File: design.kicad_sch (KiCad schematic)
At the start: 0 parts

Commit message: add TPS61099
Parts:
- added U1: TPS61099YFFT, BGA6N40P3X2_122X88X62N, symbol Converter_DCDC_custom:TPS61099YFFT
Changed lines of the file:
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@@
     (comment 4 "<<hash>>")
+  )
+  (symbol (lib_id "Converter_DCDC_custom:TPS61099YFFT") (at 147.32 88.9 0) (unit 1)
+    (in_bom yes) (on_board yes) (fields_autoplaced)
+    (property "Reference" "U1" (id 0) (at 147.32 76.2 0))
+    (property "Value" "TPS61099YFFT" (id 1) (at 147.32 78.74 0))
+    (property "Footprint" "BGA6N40P3X2_122X88X62N" (id 2) (at 147.32 81.28 0)
+      (effects (font (size 1.27 1.27)) (justify left bottom) hide)
+    )
+    (property "Datasheet" "" (id 3) (at 147.32 88.9 0)
+      (effects (font (size 1.27 1.27)) (justify left bottom) hide)
+    )
+    (property "STANDARD" "IPC 7351B" (id 4) (at 147.32 73.66 0)
+      (effects (font (size 1.27 1.27)) (justify left bottom) hide)
+    )
+    (property "PARTREV" "K" (id 5) (at 144.78 76.2 0)
+      (effects (font (size 1.27 1.27)) (justify left bottom) hide)
+    )
+    (property "MAXIMUM_PACKAGE_HEIGHT" "0.625mm" (id 6) (at 147.32 76.2 0)
+      (effects (font (size 1.27 1.27)) (justify left bottom) hide)
+    )
+    (property "MANUFACTURER" "Texas Instruments" (id 7) (at 147.32 78.74 0)
+      (effects (font (size 1.27 1.27)) (justify left bottom) hide)
+    )
+    (pin "A1")
+    (pin "A2")
+    (pin "B1")
+    (pin "B2")
+    (pin "C1")
+    (pin "C2")
   )
   (sheet_instances
     (path "/" (page "1"))
   )
+  (symbol_instances
+    (path "/63f96008-1e4e-43d2-a021-cfff672ef086"
+      (reference "U1") (unit 1) (value "TPS61099YFFT") (footprint "BGA6N40P3X2_122X88X62N")
+    )
+  )
 )

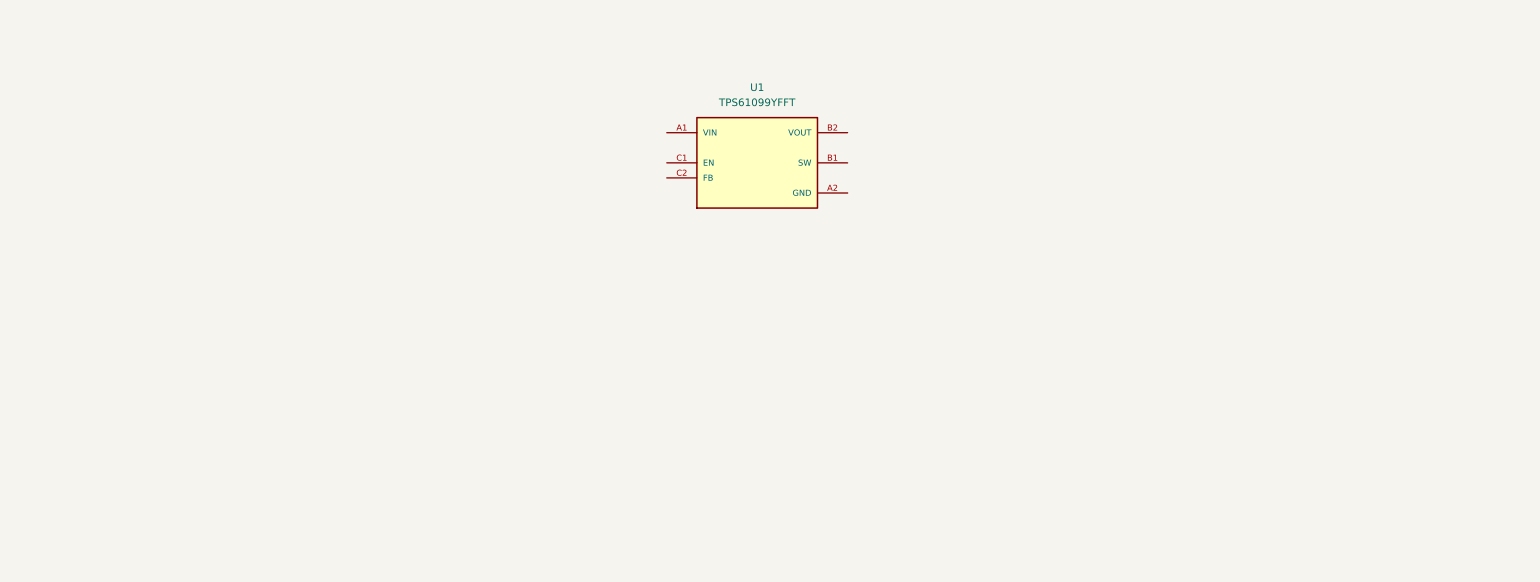
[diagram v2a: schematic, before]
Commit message: SCH/PCB Add initial design
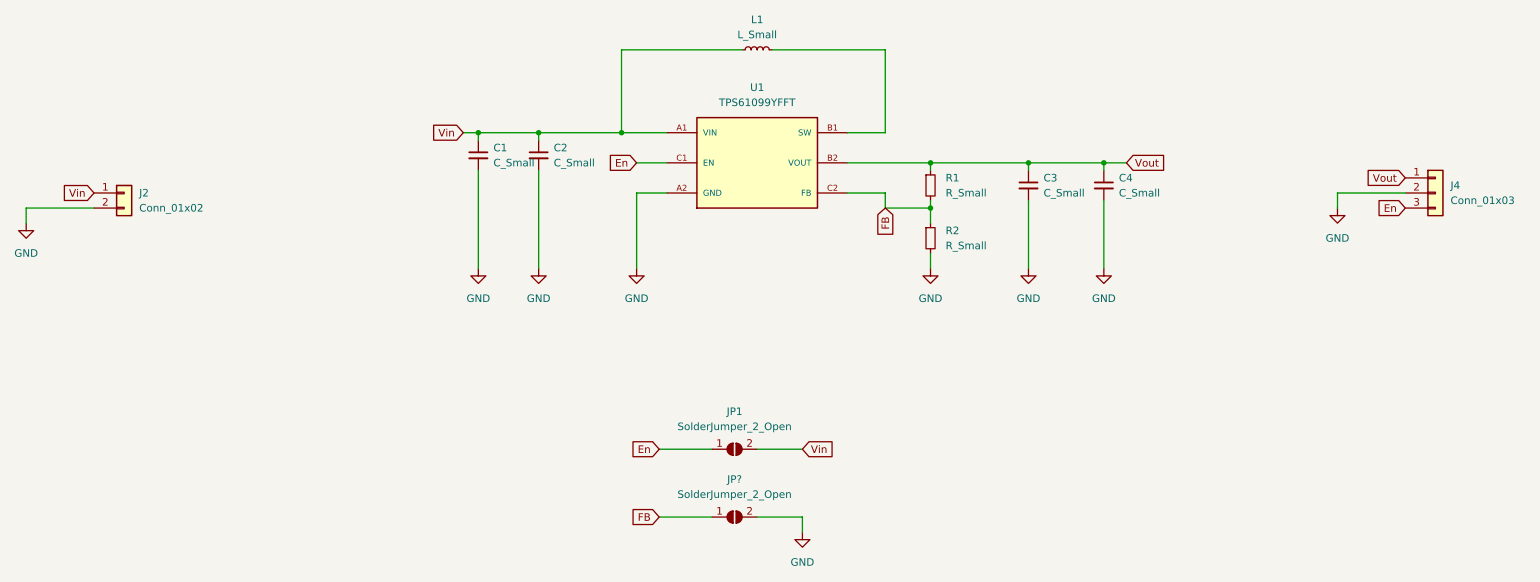
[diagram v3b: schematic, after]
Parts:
- added C1, C2, C3, C4: C_Small, Capacitor_SMD:C_0805_2012Metric, symbol Device:C_Small
- added J2: Conn_01x02, Connector_PinHeader_2.54mm:PinHeader_1x02_P2.54mm_Vertical, symbol Connector_Generic:Conn_01x02
- added J4: Conn_01x03, Connector_PinHeader_2.54mm:PinHeader_1x03_P2.54mm_Vertical, symbol Connector_Generic:Conn_01x03
- added JP1, JP?: SolderJumper_2_Open, Jumper:SolderJumper-2_P1.3mm_Open_RoundedPad1.0x1.5mm, symbol Jumper:SolderJumper_2_Open
- added L1: L_Small, Inductor_SMD:L_1008_2520Metric, symbol Device:L_Small
- added R1, R2: R_Small, Resistor_SMD:R_0805_2012Metric, symbol Device:R_Small
- U1: footprint BGA6N40P3X2_122X88X62N -> Converter_DCDC_custom:BGA6N40P3X2_122X88X62N
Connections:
- net Vin: now reaches U1.A1 (VIN)
- net Vin: now also C1.1, C2.1, J2.1 (Pin_1), JP1.2 (B), L1.1
- net GND: now reaches U1.A2 (GND)
- net GND: now also C1.2, C2.2, C3.2, C4.2, J2.2 (Pin_2), J4.2 (Pin_2), JP?.2 (B), R2.2
- net at U1.B1 (SW): now also L1.2
- net Vout: now reaches U1.B2 (VOUT)
- net Vout: now also C3.1, C4.1, J4.1 (Pin_1), R1.1
- net En: now reaches U1.C1 (EN)
- net En: now also J4.3 (Pin_3), JP1.1 (A)
- net FB: now reaches U1.C2 (FB)
- net FB: now also JP?.1 (A), R1.2, R2.1

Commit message: SCH/PCB desin according Datasheet
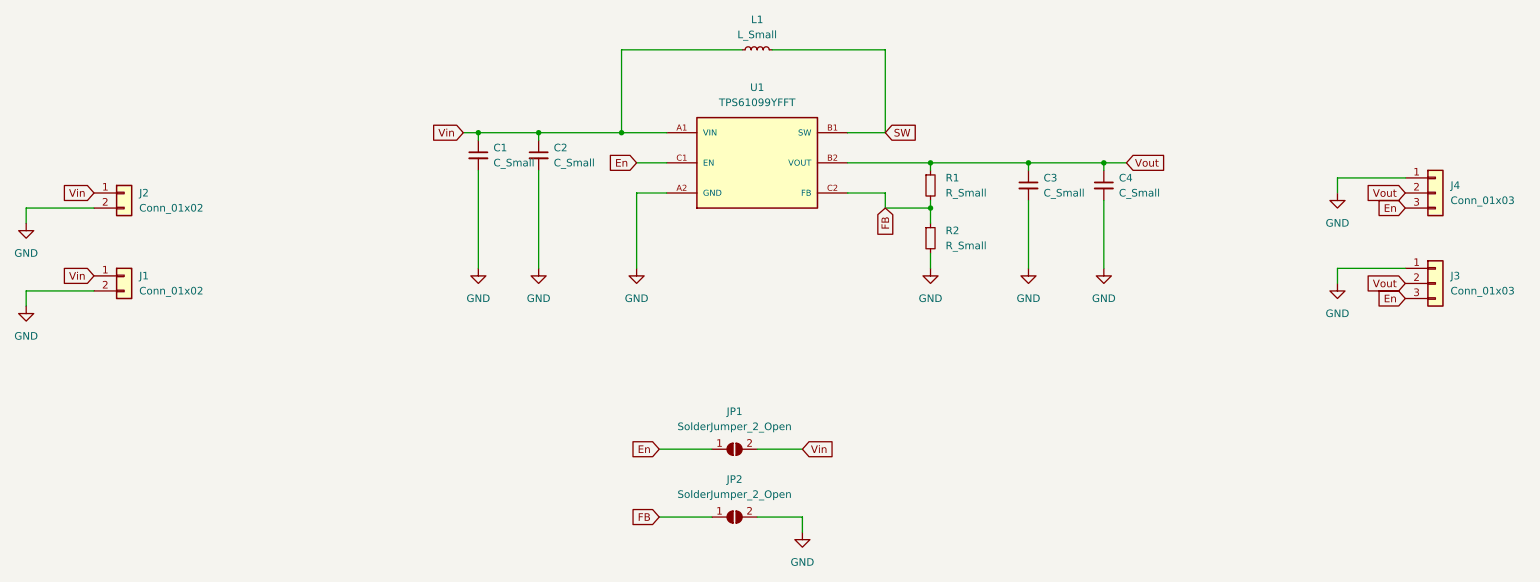
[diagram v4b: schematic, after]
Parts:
- added J1: Conn_01x02, Connector_PinHeader_2.54mm:PinHeader_1x02_P2.54mm_Vertical, symbol Connector_Generic:Conn_01x02
- added J3: Conn_01x03, Connector_PinHeader_2.54mm:PinHeader_1x03_P2.54mm_Vertical, symbol Connector_Generic:Conn_01x03
- gave numbers to parts that had none: 1
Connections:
- net En: now also J3.3 (Pin_3)
- net GND: now also J4.1 (Pin_1), J1.2 (Pin_2), J3.1 (Pin_1); no longer J4.2 (Pin_2)
- net Vin: now also J1.1 (Pin_1)
- net Vout: now also J4.2 (Pin_2), J3.2 (Pin_2); no longer J4.1 (Pin_1)
- net SW: now reaches L1.2, U1.B1 (SW)
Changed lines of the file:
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@@
+    (stroke (width 0) (type default) (color 0 0 0 0))
+  )
+  (wire (pts (xy 245.11 109.22) (xy 245.11 106.68))
+    (stroke (width 0) (type default) (color 0 0 0 0))
+  )
+  (wire (pts (xy 24.13 113.03) (xy 24.13 110.49))
     (stroke (width 0) (type default) (color 0 0 0 0))
   )
@@
     (stroke (width 0) (type default) (color 0 0 0 0))
   )
+  (wire (pts (xy 24.13 110.49) (xy 35.56 110.49))
+    (stroke (width 0) (type default) (color 0 0 0 0))
+  )
   (wire (pts (xy 124.46 69.85) (xy 124.46 83.82))
     (stroke (width 0) (type default) (color 0 0 0 0))
@@
     (stroke (width 0) (type default) (color 0 0 0 0))
   )
-  (wire (pts (xy 245.11 93.98) (xy 256.54 93.98))
+  (wire (pts (xy 245.11 91.44) (xy 256.54 91.44))
     (stroke (width 0) (type default) (color 0 0 0 0))
   )
@@
     (stroke (width 0) (type default) (color 0 0 0 0))
   )
+  (wire (pts (xy 245.11 106.68) (xy 256.54 106.68))
+    (stroke (width 0) (type default) (color 0 0 0 0))
+  )
   (wire (pts (xy 124.46 83.82) (xy 132.08 83.82))
     (stroke (width 0) (type default) (color 0 0 0 0))
@@
     (stroke (width 0) (type default) (color 0 0 0 0))
   )
-  (wire (pts (xy 245.11 96.52) (xy 245.11 93.98))
+  (wire (pts (xy 245.11 93.98) (xy 245.11 91.44))
     (stroke (width 0) (type default) (color 0 0 0 0))
   )
@@
     (effects (font (size 1.27 1.27)) (justify right))
     (property "Intersheet References" "${INTERSHEET_REFS}" (id 0) (at 92.6234 83.7406 0)
+      (effects (font (size 1.27 1.27)) (justify right) hide)
+    )
+  )
+  (global_label "SW" (shape input) (at 168.91 83.82 0) (fields_autoplaced)
+    (effects (font (size 1.27 1.27)) (justify left))
+    (property "Intersheet References" "${INTERSHEET_REFS}" (id 0) (at 173.8952 83.7406 0)
+      (effects (font (size 1.27 1.27)) (justify left) hide)
+    )
+  )
+  (global_label "Vout" (shape input) (at 256.54 109.22 180) (fields_autoplaced)
+    (effects (font (size 1.27 1.27)) (justify right))
+    (property "Intersheet References" "${INTERSHEET_REFS}" (id 0) (at 250.1034 109.2994 0)
       (effects (font (size 1.27 1.27)) (justify right) hide)
     )
@@
     )
   )
+  (global_label "En" (shape input) (at 256.54 111.76 180) (fields_autoplaced)
+    (effects (font (size 1.27 1.27)) (justify right))
+    (property "Intersheet References" "${INTERSHEET_REFS}" (id 0) (at 251.9177 111.6806 0)
+      (effects (font (size 1.27 1.27)) (justify right) hide)
+    )
+  )
+  (global_label "Vin" (shape input) (at 35.56 107.95 180) (fields_autoplaced)
+    (effects (font (size 1.27 1.27)) (justify right))
+    (property "Intersheet References" "${INTERSHEET_REFS}" (id 0) (at 30.3934 107.8706 0)
+      (effects (font (size 1.27 1.27)) (justify right) hide)
+    )
+  )
   (global_label "Vout" (shape input) (at 209.55 88.9 0) (fields_autoplaced)
     (effects (font (size 1.27 1.27)) (justify left))
@@
     )
   )
-  (global_label "Vout" (shape input) (at 256.54 91.44 180) (fields_autoplaced)
-    (effects (font (size 1.27 1.27)) (justify right))
-    (property "Intersheet References" "${INTERSHEET_REFS}" (id 0) (at 250.1034 91.5194 0)
+  (global_label "Vout" (shape input) (at 256.54 93.98 180) (fields_autoplaced)
+    (effects (font (size 1.27 1.27)) (justify right))
+    (property "Intersheet References" "${INTERSHEET_REFS}" (id 0) (at 250.1034 94.0594 0)
       (effects (font (size 1.27 1.27)) (justify right) hide)
     )
@@
     (pin "2")
   )
+  (symbol (lib_id "power:GND") (at 24.13 113.03 0) (unit 1)
+    (in_bom yes) (on_board yes) (fields_autoplaced)
+    (property "Reference" "#PWR0105" (id 0) (at 24.13 119.38 0)
+      (effects (font (size 1.27 1.27)) hide)
+    )
+    (property "Value" "GND" (id 1) (at 24.13 118.11 0))
+    (property "Footprint" "" (id 2) (at 24.13 113.03 0)
+      (effects (font (size 1.27 1.27)) hide)
+    )
+    (property "Datasheet" "" (id 3) (at 24.13 113.03 0)
+      (effects (font (size 1.27 1.27)) hide)
+    )
+    (pin "1")
+  )
   (symbol (lib_id "Jumper:SolderJumper_2_Open") (at 143.51 148.59 0) (unit 1)
     (in_bom yes) (on_board yes) (fields_autoplaced)
-    (property "Reference" "JP?" (id 0) (at 143.51 142.24 0))
+    (property "Reference" "JP2" (id 0) (at 143.51 142.24 0))
     (property "Value" "SolderJumper_2_Open" (id 1) (at 143.51 144.78 0))
     (property "Footprint" "Jumper:SolderJumper-2_P1.3mm_Open_RoundedPad1.0x1.5mm" (id 2) (at 143.51 148.59 0)
@@
     (pin "1")
     (pin "2")
+  )
+  (symbol (lib_id "Connector_Generic:Conn_01x03") (at 261.62 109.22 0) (unit 1)
+    (in_bom yes) (on_board yes) (fields_autoplaced)
+    (property "Reference" "J3" (id 0) (at 264.16 107.9499 0)
+      (effects (font (size 1.27 1.27)) (justify left))
+    )
+    (property "Value" "Conn_01x03" (id 1) (at 264.16 110.4899 0)
+      (effects (font (size 1.27 1.27)) (justify left))
+    )
+    (property "Footprint" "Connector_PinHeader_2.54mm:PinHeader_1x03_P2.54mm_Vertical" (id 2) (at 261.62 109.22 0)
+      (effects (font (size 1.27 1.27)) hide)
+    )
+    (property "Datasheet" "~" (id 3) (at 261.62 109.22 0)
+      (effects (font (size 1.27 1.27)) hide)
+    )
+    (pin "1")
+    (pin "2")
+    (pin "3")
   )
   (symbol (lib_id "power:GND") (at 193.04 106.68 0) (unit 1)
@@
     (pin "2")
   )
-  (symbol (lib_id "power:GND") (at 245.11 96.52 0) (unit 1)
-    (in_bom yes) (on_board yes) (fields_autoplaced)
-    (property "Reference" "#PWR0101" (id 0) (at 245.11 102.87 0)
-      (effects (font (size 1.27 1.27)) hide)
-    )
-    (property "Value" "GND" (id 1) (at 245.11 101.6 0))
-    (property "Footprint" "" (id 2) (at 245.11 96.52 0)
-      (effects (font (size 1.27 1.27)) hide)
-    )
-    (property "Datasheet" "" (id 3) (at 245.11 96.52 0)
+  (symbol (lib_id "power:GND") (at 245.11 93.98 0) (unit 1)
+    (in_bom yes) (on_board yes) (fields_autoplaced)
+    (property "Reference" "#PWR0101" (id 0) (at 245.11 100.33 0)
+      (effects (font (size 1.27 1.27)) hide)
+    )
+    (property "Value" "GND" (id 1) (at 245.11 99.06 0))
+    (property "Footprint" "" (id 2) (at 245.11 93.98 0)
+      (effects (font (size 1.27 1.27)) hide)
+    )
+    (property "Datasheet" "" (id 3) (at 245.11 93.98 0)
       (effects (font (size 1.27 1.27)) hide)
     )
@@
   (symbol (lib_id "power:GND") (at 154.94 151.13 0) (unit 1)
     (in_bom yes) (on_board yes) (fields_autoplaced)
-    (property "Reference" "#PWR?" (id 0) (at 154.94 157.48 0)
+    (property "Reference" "#PWR0102" (id 0) (at 154.94 157.48 0)
       (effects (font (size 1.27 1.27)) hide)
     )
@@
     (pin "1")
   )
+  (symbol (lib_id "power:GND") (at 245.11 109.22 0) (unit 1)
+    (in_bom yes) (on_board yes) (fields_autoplaced)
+    (property "Reference" "#PWR0103" (id 0) (at 245.11 115.57 0)
+      (effects (font (size 1.27 1.27)) hide)
+    )
+    (property "Value" "GND" (id 1) (at 245.11 114.3 0))
+    (property "Footprint" "" (id 2) (at 245.11 109.22 0)
+      (effects (font (size 1.27 1.27)) hide)
+    )
+    (property "Datasheet" "" (id 3) (at 245.11 109.22 0)
+      (effects (font (size 1.27 1.27)) hide)
+    )
+    (pin "1")
+  )
   (symbol (lib_id "Connector_Generic:Conn_01x02") (at 40.64 93.98 0) (unit 1)
     (in_bom yes) (on_board yes) (fields_autoplaced)
@@
     (pin "2")
   )
+  (symbol (lib_id "Connector_Generic:Conn_01x02") (at 40.64 107.95 0) (unit 1)
+    (in_bom yes) (on_board yes) (fields_autoplaced)
+    (property "Reference" "J1" (id 0) (at 43.18 107.9499 0)
+      (effects (font (size 1.27 1.27)) (justify left))
+    )
+    (property "Value" "Conn_01x02" (id 1) (at 43.18 110.4899 0)
+      (effects (font (size 1.27 1.27)) (justify left))
+    )
+    (property "Footprint" "Connector_PinHeader_2.54mm:PinHeader_1x02_P2.54mm_Vertical" (id 2) (at 40.64 107.95 0)
+      (effects (font (size 1.27 1.27)) hide)
+    )
+    (property "Datasheet" "~" (id 3) (at 40.64 107.95 0)
+      (effects (font (size 1.27 1.27)) hide)
+    )
+    (pin "1")
+    (pin "2")
+  )
   (symbol (lib_id "Device:C_Small") (at 193.04 92.71 0) (unit 1)
     (in_bom yes) (on_board yes) (fields_autoplaced)
@@
       (reference "#PWR0101") (unit 1) (value "GND") (footprint "")
     )
+    (path "/877addf7-6029-43ff-b03b-6d8e69abce0a"
+      (reference "#PWR0102") (unit 1) (value "GND") (footprint "")
+    )
+    (path "/94420d36-ded9-4c64-ac5c-a7afff70ec70"
+      (reference "#PWR0103") (unit 1) (value "GND") (footprint "")
+    )
     (path "/8e791c9b-0679-43d5-b124-34a2af0cfe6e"
       (reference "#PWR0104") (unit 1) (value "GND") (footprint "")
     )
-    (path "/877addf7-6029-43ff-b03b-6d8e69abce0a"
-      (reference "#PWR?") (unit 1) (value "GND") (footprint "")
+    (path "/3a7372df-1a16-441a-ab1c-f73cc7118a91"
+      (reference "#PWR0105") (unit 1) (value "GND") (footprint "")
     )
     (path "/6ee7801d-5e88-4183-a12b-f744d6876270"
@@
       (reference "C4") (unit 1) (value "C_Small") (footprint "Capacitor_SMD:C_0805_2012Metric")
     )
+    (path "/f079a243-d5b2-4d0c-a10e-0770b99f59a8"
+      (reference "J1") (unit 1) (value "Conn_01x02") (footprint "Connector_PinHeader_2.54mm:PinHeader_1x02_P2.54mm_Vertical")
+    )
     (path "/99bd7f69-e007-4523-a21b-a75557f73c96"
       (reference "J2") (unit 1) (value "Conn_01x02") (footprint "Connector_PinHeader_2.54mm:PinHeader_1x02_P2.54mm_Vertical")
     )
+    (path "/5d54df50-b677-4ef2-b007-cc1e4f7afd58"
+      (reference "J3") (unit 1) (value "Conn_01x03") (footprint "Connector_PinHeader_2.54mm:PinHeader_1x03_P2.54mm_Vertical")
+    )
     (path "/dc419cf3-ff99-4d7f-8321-3891c81b8844"
       (reference "J4") (unit 1) (value "Conn_01x03") (footprint "Connector_PinHeader_2.54mm:PinHeader_1x03_P2.54mm_Vertical")
@@
     )
     (path "/3b7dcbdc-9ce7-469b-a69d-588e9c87c6ba"
-      (reference "JP?") (unit 1) (value "SolderJumper_2_Open") (footprint "Jumper:SolderJumper-2_P1.3mm_Open_RoundedPad1.0x1.5mm")
+      (reference "JP2") (unit 1) (value "SolderJumper_2_Open") (footprint "Jumper:SolderJumper-2_P1.3mm_Open_RoundedPad1.0x1.5mm")
     )
     (path "/e0423aae-62f6-458e-bfc3-807f66691924"
